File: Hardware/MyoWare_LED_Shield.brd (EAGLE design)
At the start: 52.3 x 21.8 mm, 27 parts, among them U1 MCP73831, U2 LM3914V

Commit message: Moved charge LEDs to back of board from easier manufacturing
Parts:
- moved D1 0.44 mm to (48.6, 17.8), flipped to the bottom, turned to 90 degrees
- moved D2 0.38 mm to (48.6, 15.9), flipped to the bottom, turned to 90 degrees
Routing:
- net N$15: track 21.5 -> 22.4 mm, vias 1 -> 2
- net N$9: track 4.25 -> 4.45 mm, vias 1 -> 0
- net N$10: track 3.35 -> 3.45 mm, vias 1 -> 0
- net GND: vias 10 -> 12
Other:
- board text added: "v03"
- board text removed: "v02"
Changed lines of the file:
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@@
 <?xml version="1.0" encoding="utf-8"?>
 <!DOCTYPE eagle SYSTEM "eagle.dtd">
-<eagle version="7.4.0">
+<eagle version="7.5.0">
 <drawing>
 <settings>
@@
 <text x="48.70835" y="5.774646875" size="1.27" layer="22" ratio="20" rot="R135" align="center-left">+</text>
 <text x="46.82195" y="4.041546875" size="1.27" layer="22" ratio="17" rot="R135" align="center-left">-</text>
-<text x="47.244" y="19.304" size="0.8128" layer="21" font="vector" ratio="17" align="center-left">CHG</text>
-<text x="47.244" y="15.113" size="0.8128" layer="21" font="vector" ratio="17" align="center-left">DONE</text>
+<text x="48.5775" y="18.415" size="0.8128" layer="22" font="vector" ratio="17" rot="MR0" align="bottom-center">CHG</text>
+<text x="48.5775" y="15.2146" size="0.8128" layer="22" font="vector" ratio="17" rot="MR0" align="top-center">DONE</text>
 <text x="18.288" y="-11.684" size="1.778" layer="51" font="vector">Brian E Kaminski of Advancer Technologies</text>
 <text x="-0.762" y="-14.478" size="1.778" layer="51" font="vector">Revised by: Brent Wilkins</text>
-<text x="44.7548" y="0.4318" size="1.27" layer="16" font="vector" ratio="20" rot="MR0">v02</text>
+<text x="44.7548" y="0.4318" size="1.27" layer="16" font="vector" ratio="20" rot="MR0">v03</text>
 <text x="48.9458" y="6.2484" size="1.27" layer="21" ratio="20" rot="R180" align="center-left">+</text>
 <text x="48.0314" y="4.6482" size="1.27" layer="21" ratio="17" rot="R180" align="center-left">-</text>
@@
 <attribute name="PROD_ID" value="CAP-08280" x="43.561" y="20.1295" size="1.778" layer="28" font="vector" ratio="15" rot="MR180" display="off"/>
 </element>
-<element name="D1" library="SparkFun-LED" package="LED-0603" value="RED" x="48.5775" y="18.2245" rot="R270">
-<attribute name="PROD_ID" value="DIO-00819" x="48.5775" y="18.2245" size="1.778" layer="27" font="vector" ratio="15" rot="R270" display="off"/>
+<element name="D1" library="SparkFun-LED" package="LED-0603" value="RED" x="48.5775" y="17.78" rot="MR90">
+<attribute name="PROD_ID" value="DIO-00819" x="48.5775" y="17.78" size="1.778" layer="28" font="vector" ratio="15" rot="MR90" display="off"/>
 </element>
 <element name="U1" library="SparkFun-PowerIC" package="SOT23-5" value="MCP73831" x="38.989" y="17.7165" rot="MR90">
@@
 </element>
 <element name="JP3" library="SparkFun-Connectors" package="1X02_NO_SILK" value="LiPo" x="49.4665" y="5.0165" rot="R225"/>
-<element name="D2" library="SparkFun-LED" package="LED-0603" value="RED" x="48.5775" y="16.3195" rot="R270">
-<attribute name="PROD_ID" value="DIO-00819" x="48.5775" y="16.3195" size="1.778" layer="27" rot="R270" display="off"/>
+<element name="D2" library="SparkFun-LED" package="LED-0603" value="RED" x="48.5775" y="15.9385" rot="MR90">
+<attribute name="PROD_ID" value="DIO-00819" x="48.5775" y="15.9385" size="1.778" layer="28" rot="MR90" display="off"/>
 </element>
 <element name="R5" library="SparkFun-Resistors" package="0603-RES" value="330" x="43.561" y="14.351" rot="MR180">
@@
 <via x="33.9976" y="21.0222" extent="1-16" drill="0.508"/>
 <wire x1="27.432" y1="18.288" x2="27.432" y2="17.4498" width="0.254" layer="16"/>
+<via x="39.0649" y="20.9841" extent="1-16" drill="0.508"/>
+<via x="36.5503" y="15.8914" extent="1-16" drill="0.508"/>
 </signal>
 <signal name="SIG">
@@
 <contactref element="R3" pad="1"/>
 <contactref element="D1" pad="A"/>
-<via x="45.974" y="18.161" extent="1-16" drill="0.6"/>
-<wire x1="44.411" y1="18.161" x2="45.974" y2="18.161" width="0.4064" layer="16"/>
-<wire x1="47.7005" y1="18.2245" x2="45.974" y2="18.2245" width="0.4064" layer="1"/>
-<wire x1="45.974" y1="18.2245" x2="45.974" y2="18.161" width="0.4064" layer="1"/>
+<wire x1="44.411" y1="18.161" x2="45.9613" y2="18.161" width="0.4064" layer="16"/>
+<wire x1="45.9613" y1="18.161" x2="46.3423" y2="17.78" width="0.4064" layer="16"/>
+<wire x1="46.3423" y1="17.78" x2="47.7005" y2="17.78" width="0.4064" layer="16"/>
 </signal>
 <signal name="N$15">
@@
 <wire x1="37.6889" y1="16.7665" x2="37.6889" y2="14.986" width="0.4064" layer="16"/>
 <contactref element="R5" pad="1"/>
-<wire x1="47.867" y1="19.812" x2="43.942" y2="19.812" width="0.4064" layer="1"/>
+<wire x1="47.7146" y1="19.812" x2="43.942" y2="19.812" width="0.4064" layer="1"/>
 <wire x1="43.1927" y1="17.5895" x2="41.402" y2="17.5895" width="0.4064" layer="1"/>
 <wire x1="41.402" y1="17.5895" x2="39.751" y2="15.9385" width="0.4064" layer="1"/>
 <wire x1="39.751" y1="15.9385" x2="39.751" y2="14.351" width="0.4064" layer="1"/>
 <wire x1="42.711" y1="14.351" x2="39.751" y2="14.351" width="0.4064" layer="16"/>
-<wire x1="47.867" y1="19.812" x2="49.4545" y2="18.2245" width="0.4064" layer="1"/>
 <wire x1="37.6889" y1="14.986" x2="38.3239" y2="14.351" width="0.4064" layer="16"/>
 <wire x1="38.3239" y1="14.351" x2="39.751" y2="14.351" width="0.4064" layer="16"/>
@@
 <wire x1="43.5102" y1="17.907" x2="43.5102" y2="19.3802" width="0.4064" layer="1"/>
 <wire x1="43.5102" y1="19.3802" x2="43.942" y2="19.812" width="0.4064" layer="1"/>
+<via x="47.7146" y="19.812" extent="1-16" drill="0.6"/>
+<wire x1="47.7146" y1="19.812" x2="48.6283" y2="19.812" width="0.4064" layer="16"/>
+<wire x1="48.6283" y1="19.812" x2="49.4545" y2="18.9858" width="0.4064" layer="16"/>
+<wire x1="49.4545" y1="18.9858" x2="49.4545" y2="17.78" width="0.4064" layer="16"/>
 </signal>
 <signal name="N$17">
@@
 <contactref element="R5" pad="2"/>
 <contactref element="D2" pad="A"/>
-<via x="45.974" y="14.351" extent="1-16" drill="0.6"/>
-<wire x1="44.411" y1="14.351" x2="45.974" y2="14.351" width="0.4064" layer="16"/>
-<wire x1="47.7005" y1="16.3195" x2="47.7005" y2="16.0775" width="0.4064" layer="1"/>
-<wire x1="47.7005" y1="16.0775" x2="45.974" y2="14.351" width="0.4064" layer="1"/>
+<wire x1="44.411" y1="14.351" x2="46.9646" y2="14.351" width="0.4064" layer="16"/>
+<wire x1="46.9646" y1="14.351" x2="47.7005" y2="15.0869" width="0.4064" layer="16"/>
+<wire x1="47.7005" y1="15.0869" x2="47.7005" y2="15.9385" width="0.4064" layer="16"/>
 </signal>
 <signal name="SHIELD">

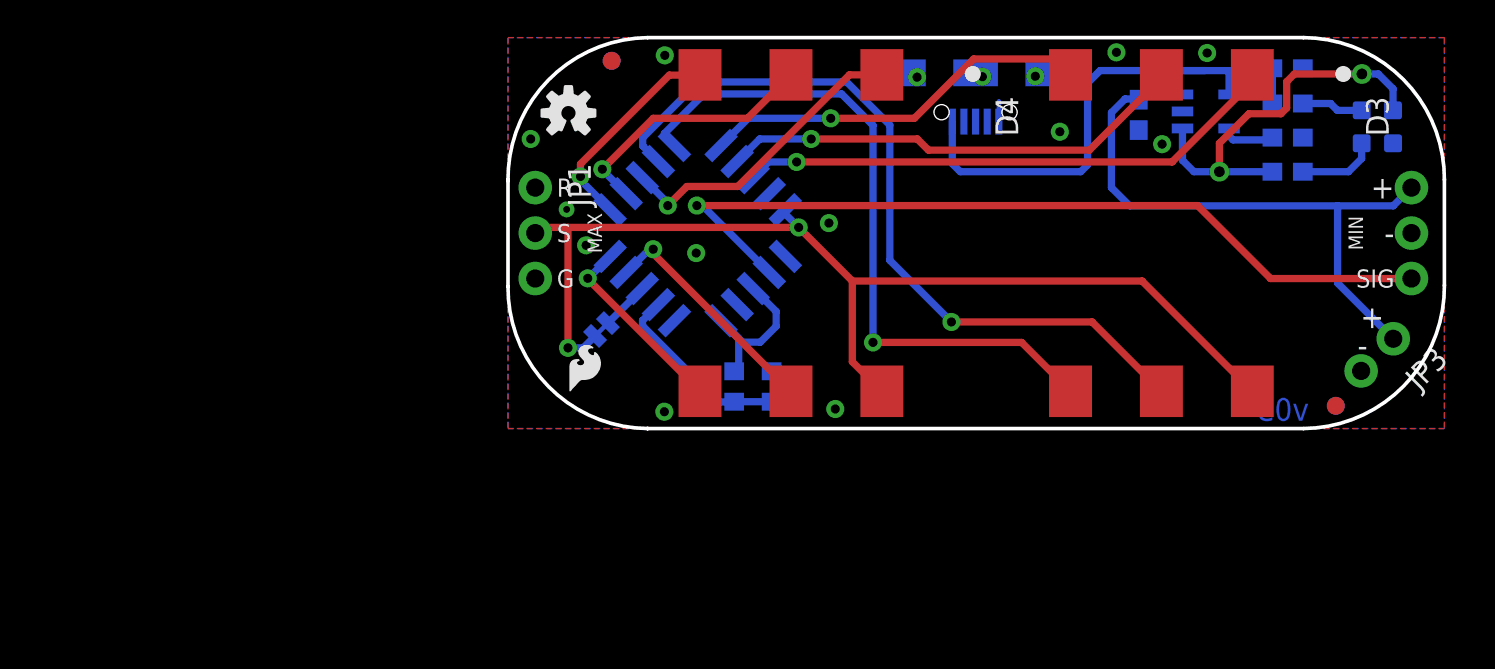
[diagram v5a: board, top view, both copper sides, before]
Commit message: Added cable header alignment in silk & minor weaks.
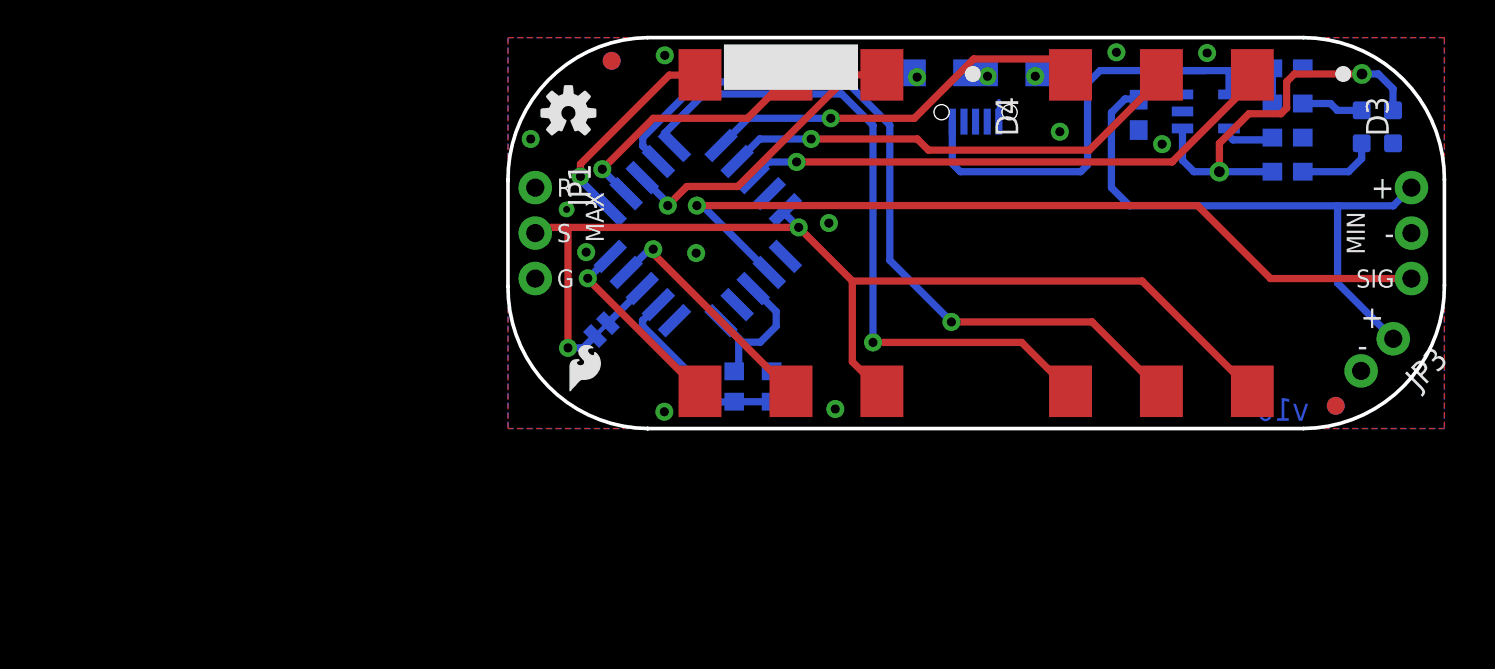
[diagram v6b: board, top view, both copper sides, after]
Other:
- board text added: "External cable connector lines up here =>"
- board text added: "v10"
- board text removed: "v03"

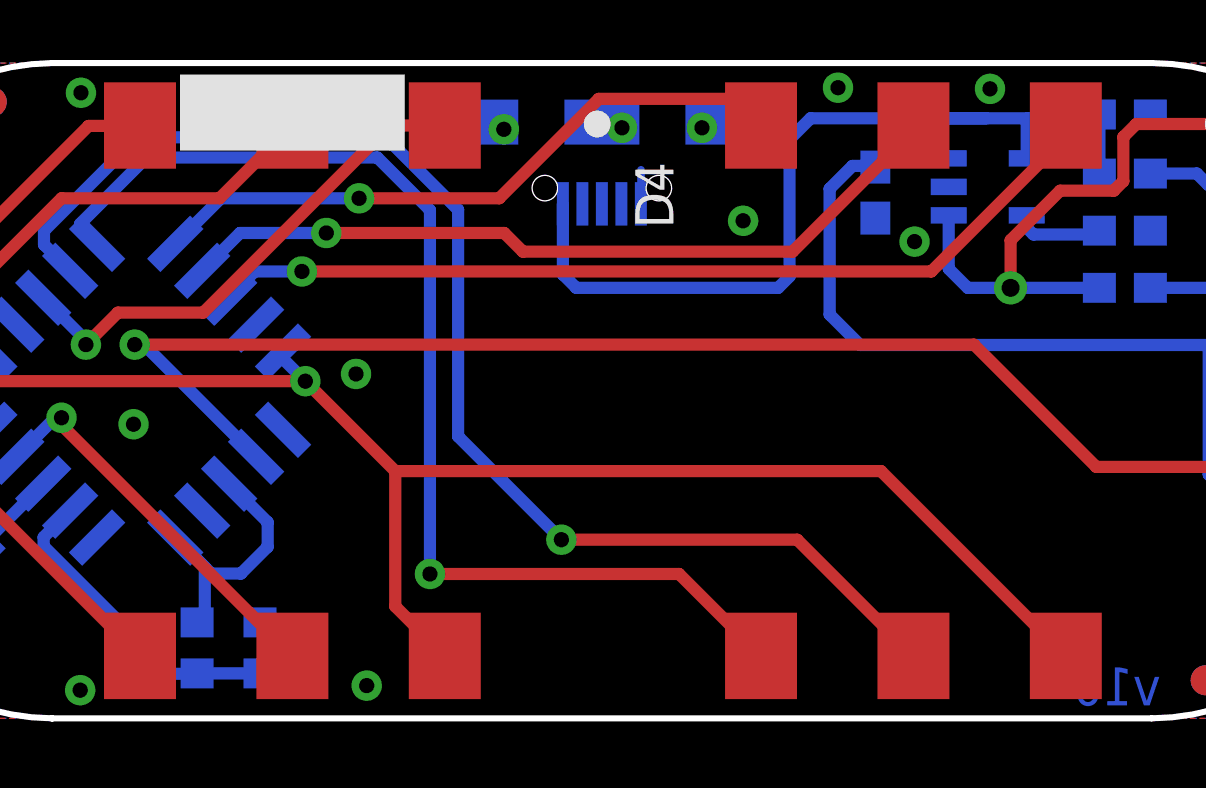
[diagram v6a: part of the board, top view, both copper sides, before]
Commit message: Improved micro-B DFM & fixed alignment silk
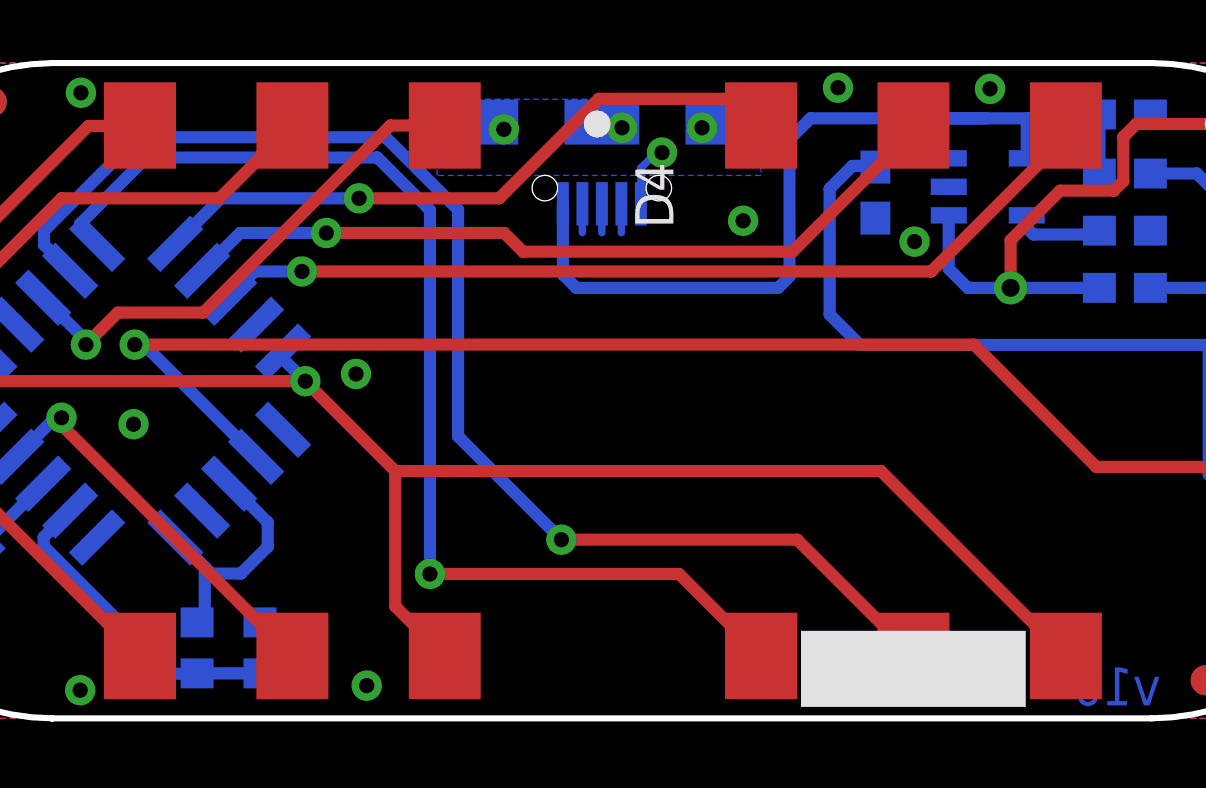
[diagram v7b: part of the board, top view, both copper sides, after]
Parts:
- moved FRAME1 3.81 mm to (-12.2, -15.5)
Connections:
- new net D+: JP4.D+
- new net D-: JP4.D-
- new net ID: JP4.ID
- new net SHIELD: JP4.SHIELD1, JP4.SHIELD2, JP4.SHIELD3
- net GND: now also JP4.GND; no longer JP4.GND1
- net VBUS: now also JP4.VBUS; no longer JP4.VBUS1
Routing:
- net SHIELD: track 0.00 -> 1.40 mm, vias 1 -> 3
- net ID: track 0.00 -> 0.96 mm
- net D-: track 0.00 -> 0.96 mm
- net D+: track 0.00 -> 0.96 mm
- net GND: track 0.84 -> 1.35 mm, vias 12 -> 13
- added copper zone on layer 16, net SHIELD
